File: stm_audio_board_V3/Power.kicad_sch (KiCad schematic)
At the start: 66 parts, among them J5 Barrel_Jack_MountingPin, U1 IS42S16100H-7TL, U13 LM7809_TO220, U16 LM7909_TO220, U2 OP275, U4 OP275, U5 MIC2920A-3.3WS-TR, U9 MIC2920A-3.3WS-TR

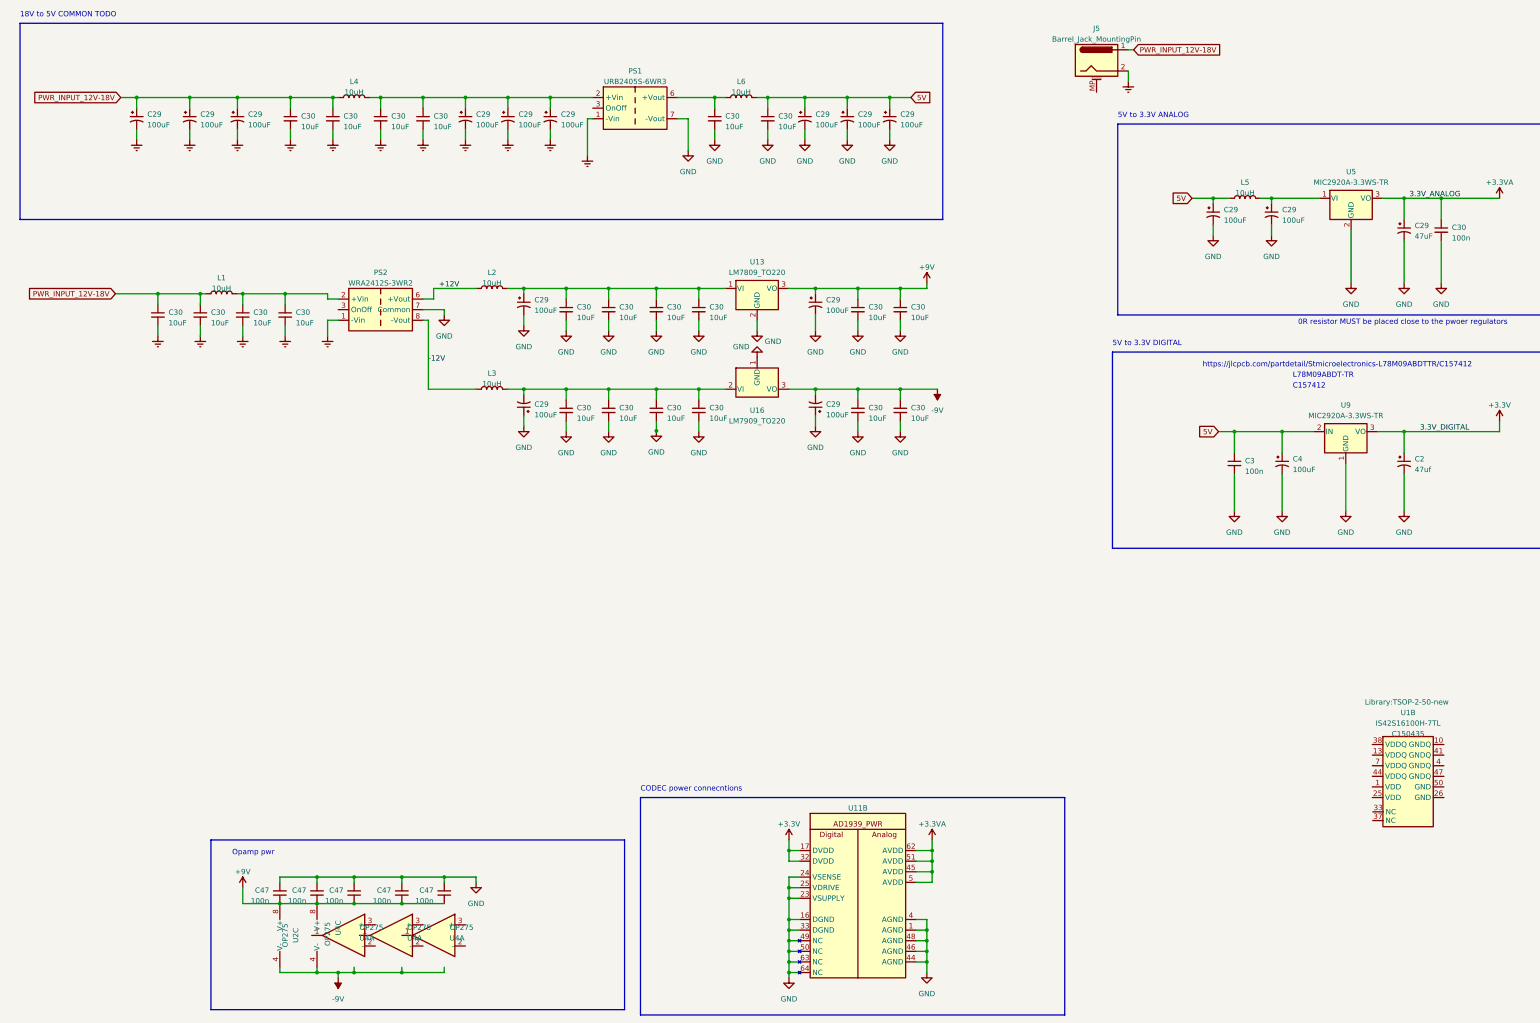
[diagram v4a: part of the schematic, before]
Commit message: Analog power and SDRAm routing reworked
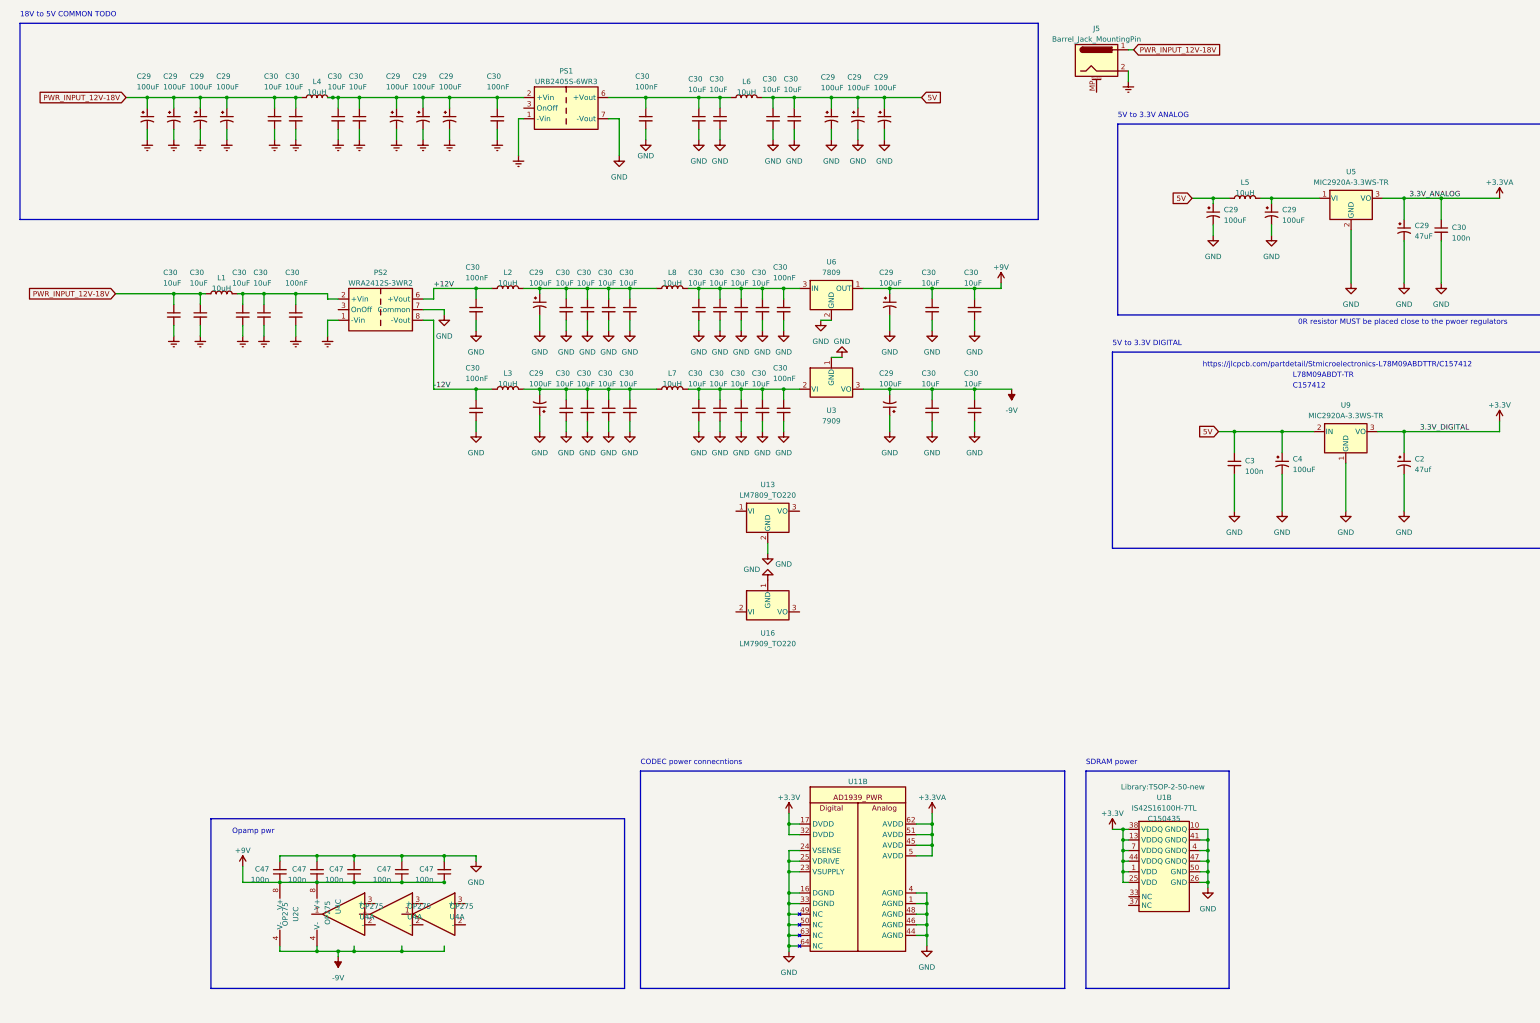
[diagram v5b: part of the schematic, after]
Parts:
- added C29: 100uF, Capacitor_THT:CP_Radial_D6.3mm_P2.50mm, symbol Device:C_Polarized_Small_US
- added C30 (x10): 10uF, Capacitor_SMD:C_1206_3216Metric, symbol Device:C_Small
- added C30 (x7): 100nF, Capacitor_SMD:C_0603_1608Metric, symbol Device:C_Small
- added L7, L8: 10uH, Inductor_SMD:L_6.3x6.3_H3, symbol Device:L
- added U3: 7909, Package_TO_SOT_SMD:SOT-89-3, symbol Regulator_Linear:L79L05_SOT89
- added U6: 7809, Package_TO_SOT_SMD:SOT-89-3, symbol Regulator_Linear:L78L09_SOT89
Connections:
- net +12V: now also C30.1
- net +3.3V: now also U1.1 (VDD), U1.13 (VDDQ), U1.25 (VDD), U1.38 (VDDQ), U1.44 (VDDQ), U1.7 (VDDQ)
- net +9V: now also U6.1 (OUT); no longer U13.3 (VO)
- net -12V: now also C30.1
- net -9V: now also U3.3 (VO); no longer U16.3 (VO)
- net 5V: now also C30.1
- net Earth: now also C29.2, C30.2, C30.2
- net GND: now also U1.10 (GNDQ), U1.26 (GND), U1.4 (GNDQ), U1.41 (GNDQ), U1.47 (GNDQ), U1.50 (GND), C30.2, C30.2, C30.2, C30.2, C30.2, C30.2, C30.2, C30.2, C30.2, C30.2, C30.2, C30.2, C30.2, C30.2, C30.2, U3.1 (GND), U6.2 (GND)
- net PWR_INPUT_12V-18V: now also C29.1
- net at C29.1, C29.1, C29.1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: now also C30.1
- net at C30.1, C30.1, L1.2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: now also C30.1
- net at C29.2, C30.1, C30.1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: now also L7.1; no longer U16.2 (VI)
- net at C30.1, L6.1, PS1.6 (+Vout): now also C30.1, C30.1
- net at C29.1, C30.1, C30.1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: now also L8.1; no longer U13.1 (VI)
- new net: C30.1, C30.1, C30.1, C30.1, C30.1, L7.2, U3.2 (VI)
- new net: C30.1, C30.1, C30.1, C30.1, C30.1, L8.2, U6.3 (IN)
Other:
- note added: "SDRAM power"
- moved on the sheet: C29, C30, C47, L2, L3, L4, L6, PS1, U11B, U13, U16, U1B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

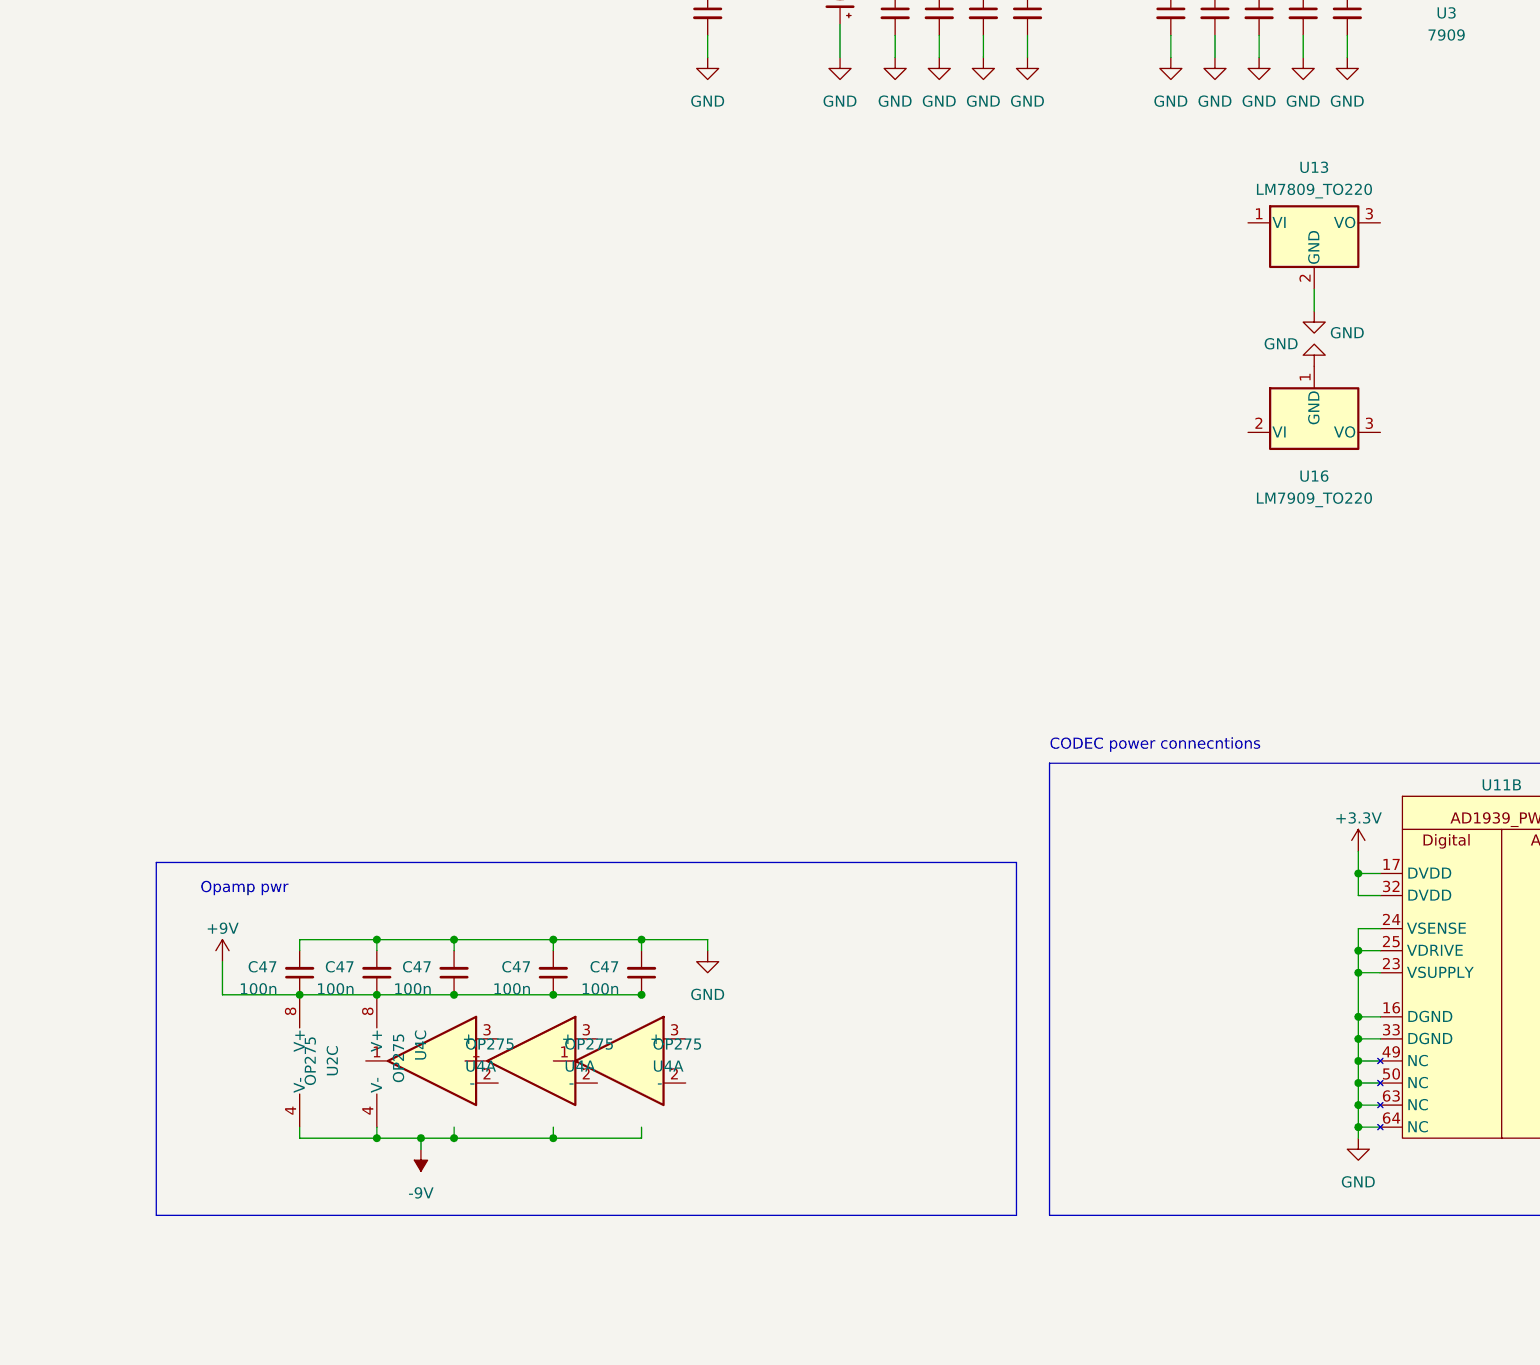
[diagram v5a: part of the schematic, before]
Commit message: Footswitch debounce added
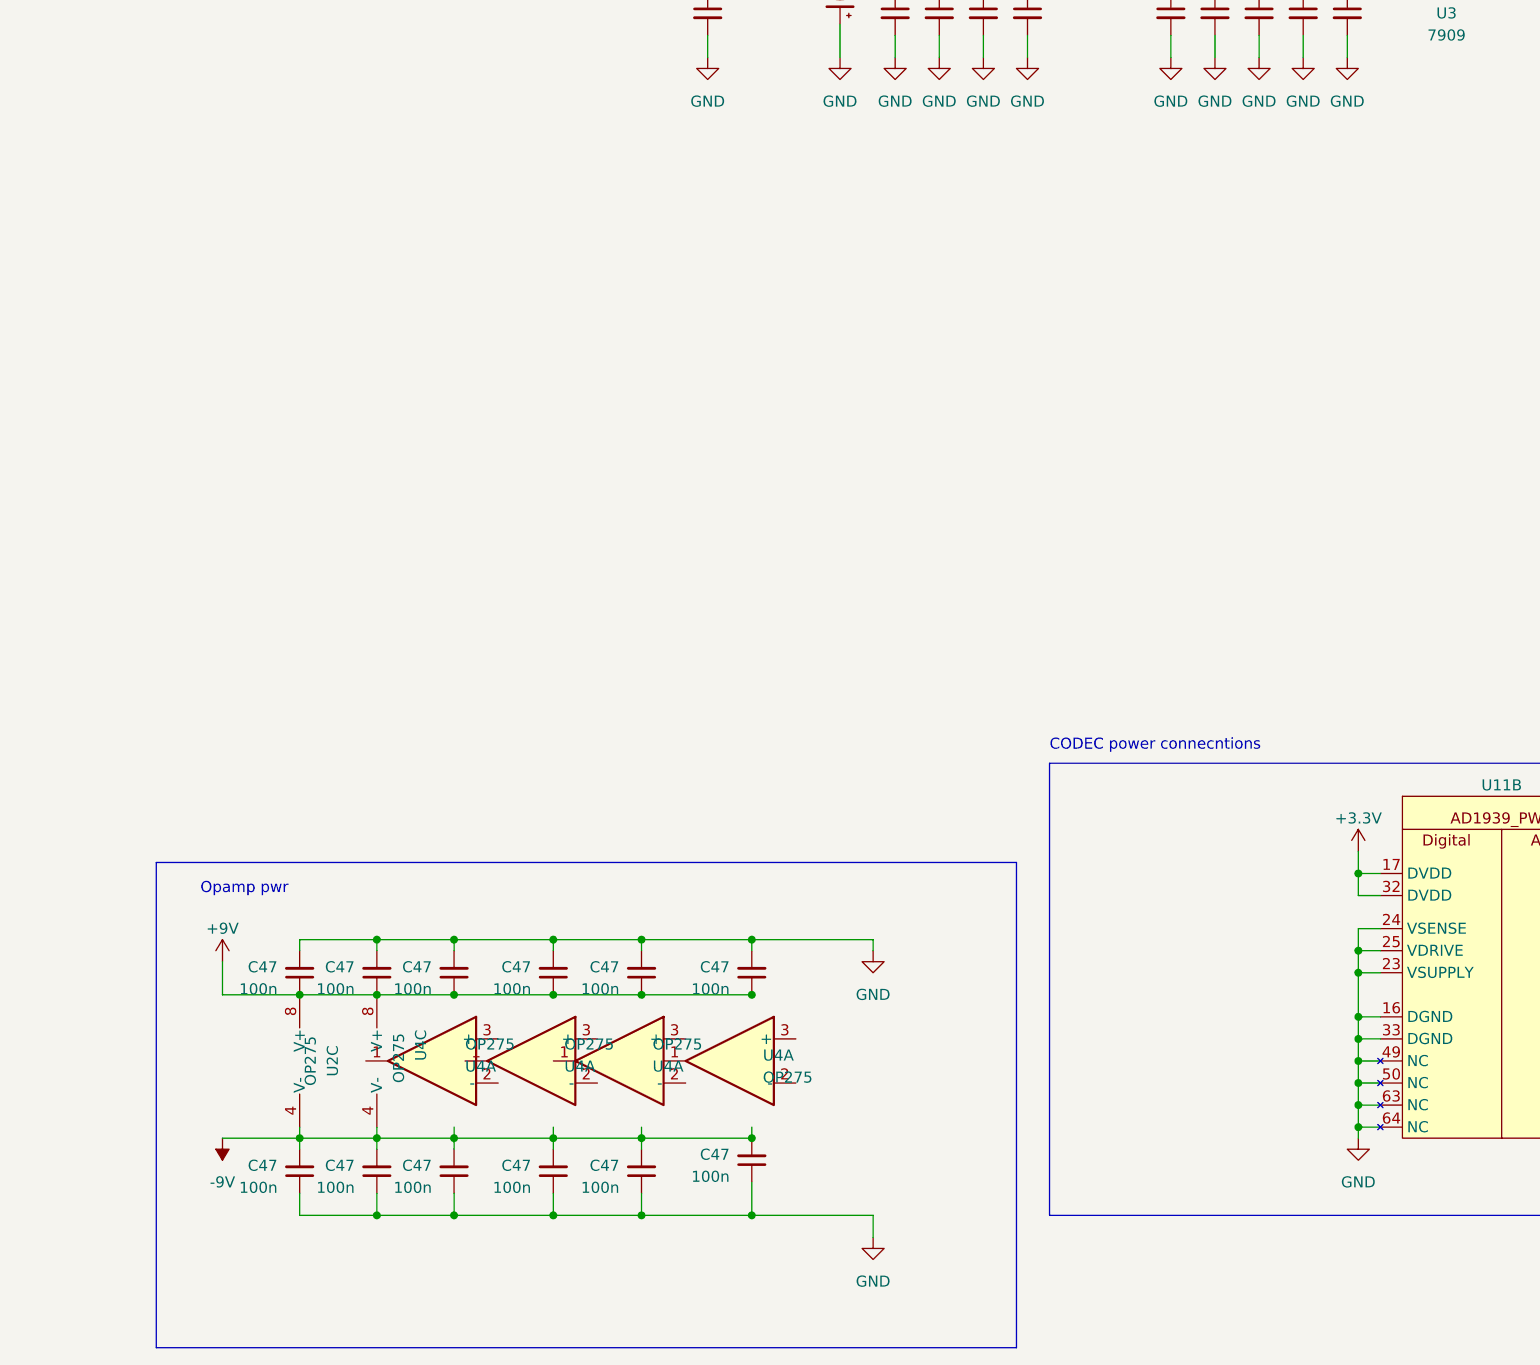
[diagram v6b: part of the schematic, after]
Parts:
- removed U13: LM7809_TO220, Package_TO_SOT_THT:TO-220-3_Vertical, symbol Regulator_Linear:LM7809_TO220
- removed U16: LM7909_TO220, Package_TO_SOT_THT:TO-220-3_Vertical, symbol Regulator_Linear:LM7909_TO220
- added C47 (x7): 100n, Capacitor_SMD:C_0603_1608Metric, symbol Device:C_Small
- added U4: OP275, Package_SO:SSOP-8_3.9x5.05mm_P1.27mm, symbol Amplifier_Operational:OP275
- L1, L2, L3, L4, L5, L6, L7, L8: footprint Inductor_SMD:L_6.3x6.3_H3 -> Inductor_SMD:L_Sunlord_SWPA6020S; JLCPCB (none) -> C242335
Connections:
- net +9V: now also C47.1
- net -9V: now also C47.2, C47.2, C47.2, C47.2, C47.2, C47.2
- net GND: now also C47.1, C47.1, C47.1, C47.1, C47.1, C47.1, C47.2

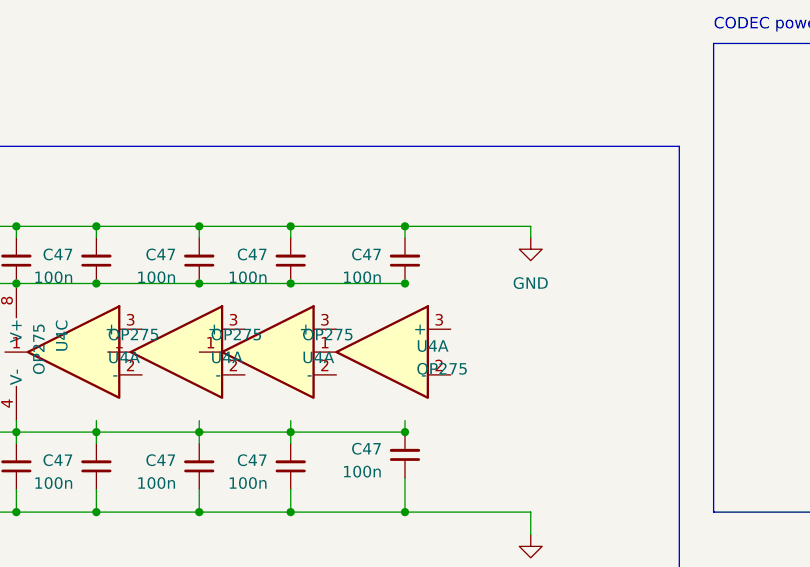
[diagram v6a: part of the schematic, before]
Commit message: USB added
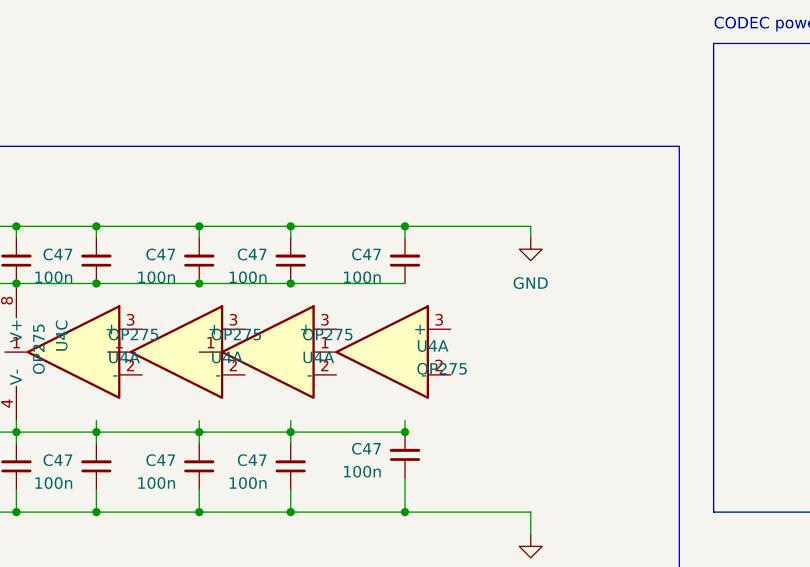
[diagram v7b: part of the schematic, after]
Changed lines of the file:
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@@
   (junction (at 181.61 107.95) (diameter 0) (color 0 0 0 0)
-  )
-  (junction (at 133.35 226.06) (diameter 0) (color 0 0 0 0)
   )
   (junction (at 247.65 83.82) (diameter 0) (color 0 0 0 0)
